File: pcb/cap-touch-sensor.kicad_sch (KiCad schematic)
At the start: 12 parts, among them U4 CAP1296-x-AIA

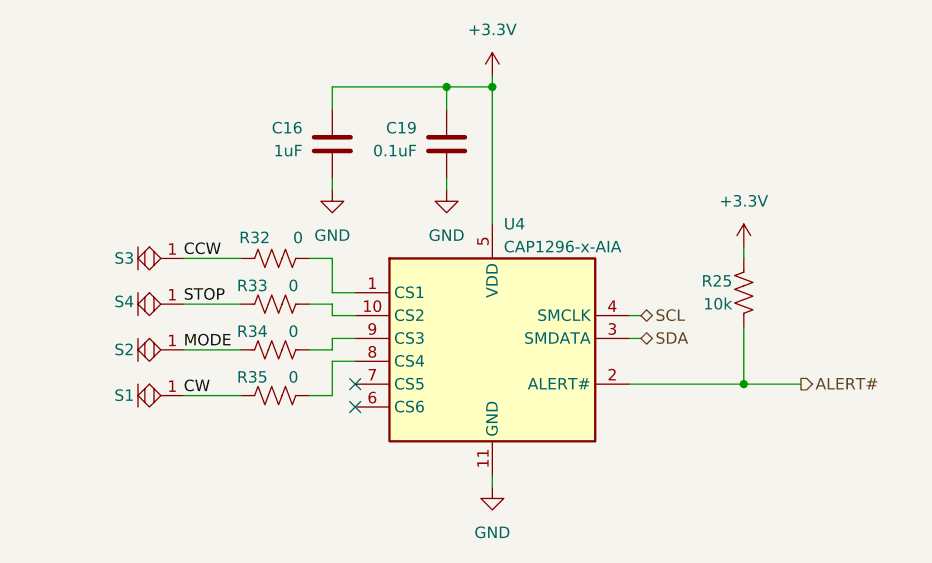
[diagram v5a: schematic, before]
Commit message: Some edits during PR review
- Silkscreen moved on board
- Get rid of value text in fab layer
- Invert TMC_EN name to indicate correct logic
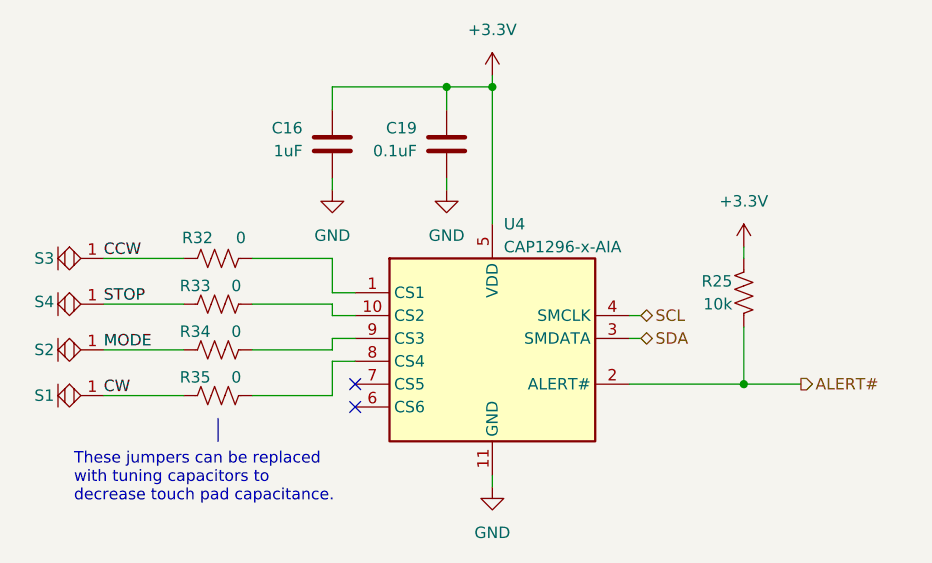
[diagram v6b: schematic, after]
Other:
- note added: "These jumpers can be replaced with tuning capacitors to decrease touch pad capacitance."
- moved on the sheet: R32, R33, R34, R35, S1, S2, S3, S4
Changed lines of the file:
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@@
 	(wire
 		(pts
-			(xy 67.31 74.93) (xy 73.66 74.93)
+			(xy 58.42 74.93) (xy 67.31 74.93)
 		)
 		(stroke
@@
 		)
 	)
+	(polyline
+		(pts
+			(xy 71.12 77.47) (xy 71.12 80.01)
+		)
+		(stroke
+			(width 0)
+			(type default)
+		)
+	)
 	(wire
 		(pts
@@
 	(wire
 		(pts
-			(xy 81.28 59.69) (xy 83.82 59.69)
+			(xy 74.93 59.69) (xy 83.82 59.69)
 		)
 		(stroke
@@
 	(wire
 		(pts
-			(xy 81.28 64.77) (xy 83.82 64.77)
+			(xy 74.93 64.77) (xy 83.82 64.77)
 		)
 		(stroke
@@
 	(wire
 		(pts
-			(xy 67.31 59.69) (xy 73.66 59.69)
+			(xy 58.42 59.69) (xy 67.31 59.69)
 		)
 		(stroke
@@
 	(wire
 		(pts
-			(xy 81.28 74.93) (xy 83.82 74.93)
-		)
-		(stroke
-			(width 0)
-			(type default)
-		)
-	)
-	(wire
-		(pts
-			(xy 67.31 64.77) (xy 73.66 64.77)
-		)
-		(stroke
-			(width 0)
-			(type default)
-		)
-	)
-	(wire
-		(pts
-			(xy 67.31 69.85) (xy 73.66 69.85)
+			(xy 74.93 74.93) (xy 83.82 74.93)
+		)
+		(stroke
+			(width 0)
+			(type default)
+		)
+	)
+	(wire
+		(pts
+			(xy 58.42 64.77) (xy 67.31 64.77)
+		)
+		(stroke
+			(width 0)
+			(type default)
+		)
+	)
+	(wire
+		(pts
+			(xy 58.42 69.85) (xy 67.31 69.85)
 		)
 		(stroke
@@
 	(wire
 		(pts
-			(xy 81.28 69.85) (xy 83.82 69.85)
+			(xy 74.93 69.85) (xy 83.82 69.85)
 		)
 		(stroke
@@
 		)
 	)
+	(text "These jumpers can be replaced\nwith tuning capacitors to \ndecrease touch pad capacitance."
+		(exclude_from_sim no)
+		(at 55.118 84.074 0)
+		(effects
+			(font
+				(size 1.27 1.27)
+			)
+			(justify left)
+		)
+	)
 	(label "MODE"
-		(at 67.31 69.85 0)
+		(at 58.42 69.85 0)
 		(fields_autoplaced yes)
 		(effects
@@
 	)
 	(label "CW"
-		(at 67.31 74.93 0)
+		(at 58.42 74.93 0)
 		(fields_autoplaced yes)
 		(effects
@@
 	)
 	(label "CCW"
-		(at 67.31 59.69 0)
+		(at 58.42 59.69 0)
 		(fields_autoplaced yes)
 		(effects
@@
 	)
 	(label "STOP"
-		(at 67.31 64.77 0)
+		(at 58.42 64.77 0)
 		(fields_autoplaced yes)
 		(effects
@@
 	(symbol
 		(lib_id "Device:R_US")
-		(at 77.47 59.69 90)
+		(at 71.12 59.69 90)
 		(unit 1)
 		(exclude_from_sim no)
@@
 		(dnp no)
 		(property "Reference" "R32"
-			(at 75.184 57.404 90)
+			(at 68.834 57.404 90)
 			(effects
 				(font
@@
 		)
 		(property "Value" "0"
-			(at 80.01 57.404 90)
+			(at 73.66 57.404 90)
 			(effects
 				(font
@@
 		)
 		(property "Footprint" "Resistor_SMD:R_0402_1005Metric"
-			(at 77.724 58.674 90)
+			(at 71.374 58.674 90)
 			(effects
 				(font
@@
 		)
 		(property "Datasheet" "~"
-			(at 77.47 59.69 0)
+			(at 71.12 59.69 0)
 			(effects
 				(font
@@
 		)
 		(property "Description" "Resistor, US symbol"
-			(at 77.47 59.69 0)
+			(at 71.12 59.69 0)
 			(effects
 				(font
@@
 	(symbol
 		(lib_id "open-ephys:TOUCH")
-		(at 64.77 64.77 90)
+		(at 55.88 64.77 90)
 		(mirror x)
 		(unit 1)
@@
 		(dnp no)
 		(property "Reference" "S4"
-			(at 60.706 64.516 90)
+			(at 51.816 64.516 90)
 			(effects
 				(font
@@
 		)
 		(property "Value" "~"
-			(at 63.5 62.23 90)
+			(at 54.61 62.23 90)
 			(effects
 				(font
@@
 		)
 		(property "Footprint" "open-ephys:Touch_Center_2mm"
-			(at 64.77 64.77 0)
+			(at 55.88 64.77 0)
 			(effects
 				(font
@@
 		)
 		(property "Datasheet" ""
-			(at 64.77 64.77 0)
+			(at 55.88 64.77 0)
 			(effects
 				(font
@@
 		)
 		(property "Description" "Printed capactitive touch sensor"
-			(at 64.77 64.77 0)
+			(at 55.88 64.77 0)
 			(effects
 				(font
@@
 	(symbol
 		(lib_id "open-ephys:TOUCH")
-		(at 64.77 69.85 90)
+		(at 55.88 69.85 90)
 		(mirror x)
 		(unit 1)
@@
 		(dnp no)
 		(property "Reference" "S2"
-			(at 60.706 69.85 90)
+			(at 51.816 69.85 90)
 			(effects
 				(font
@@
 		)
 		(property "Value" "~"
-			(at 63.5 67.31 90)
+			(at 54.61 67.31 90)
 			(effects
 				(font
@@
 		)
 		(property "Footprint" "open-ephys:Touch_Center_2mm"
-			(at 64.77 69.85 0)
+			(at 55.88 69.85 0)
 			(effects
 				(font
@@
 		)
 		(property "Datasheet" ""
-			(at 64.77 69.85 0)
+			(at 55.88 69.85 0)
 			(effects
 				(font
@@
 		)
 		(property "Description" "Printed capactitive touch sensor"
-			(at 64.77 69.85 0)
+			(at 55.88 69.85 0)
 			(effects
 				(font
@@
 	(symbol
 		(lib_id "open-ephys:TOUCH")
-		(at 64.77 59.69 90)
+		(at 55.88 59.69 90)
 		(mirror x)
 		(unit 1)
@@
 		(dnp no)
 		(property "Reference" "S3"
-			(at 60.706 59.69 90)
+			(at 51.816 59.69 90)
 			(effects
 				(font
@@
 		)
 		(property "Value" "~"
-			(at 63.5 57.15 90)
+			(at 54.61 57.15 90)
 			(effects
 				(font
@@
 		)
 		(property "Footprint" "open-ephys:Touch_Center_2mm"
-			(at 64.77 59.69 0)
+			(at 55.88 59.69 0)
 			(effects
 				(font
@@
 		)
 		(property "Datasheet" ""
-			(at 64.77 59.69 0)
+			(at 55.88 59.69 0)
 			(effects
 				(font
@@
 		)
 		(property "Description" "Printed capactitive touch sensor"
-			(at 64.77 59.69 0)
+			(at 55.88 59.69 0)
 			(effects
 				(font
@@
 	(symbol
 		(lib_id "Device:R_US")
-		(at 77.47 74.93 90)
+		(at 71.12 74.93 90)
 		(unit 1)
 		(exclude_from_sim no)
@@
 		(dnp no)
 		(property "Reference" "R35"
-			(at 74.93 72.898 90)
+			(at 68.58 72.898 90)
 			(effects
 				(font
@@
 		)
 		(property "Value" "0"
-			(at 79.502 72.898 90)
+			(at 73.152 72.898 90)
 			(effects
 				(font
@@
 		)
 		(property "Footprint" "Resistor_SMD:R_0402_1005Metric"
-			(at 77.724 73.914 90)
+			(at 71.374 73.914 90)
 			(effects
 				(font
@@
 		)
 		(property "Datasheet" "~"
-			(at 77.47 74.93 0)
+			(at 71.12 74.93 0)
 			(effects
 				(font
@@
 		)
 		(property "Description" "Resistor, US symbol"
-			(at 77.47 74.93 0)
+			(at 71.12 74.93 0)
 			(effects
 				(font
@@
 	(symbol
 		(lib_id "Device:R_US")
-		(at 77.47 69.85 90)
+		(at 71.12 69.85 90)
 		(unit 1)
 		(exclude_from_sim no)
@@
 		(dnp no)
 		(property "Reference" "R34"
-			(at 74.93 67.818 90)
+			(at 68.58 67.818 90)
 			(effects
 				(font
@@
 		)
 		(property "Value" "0"
-			(at 79.502 67.818 90)
+			(at 73.152 67.818 90)
 			(effects
 				(font
@@
 		)
 		(property "Footprint" "Resistor_SMD:R_0402_1005Metric"
-			(at 77.724 68.834 90)
+			(at 71.374 68.834 90)
 			(effects
 				(font
@@
 		)
 		(property "Datasheet" "~"
-			(at 77.47 69.85 0)
+			(at 71.12 69.85 0)
 			(effects
 				(font
@@
 		)
 		(property "Description" "Resistor, US symbol"
-			(at 77.47 69.85 0)
+			(at 71.12 69.85 0)
 			(effects
 				(font
@@
 	(symbol
 		(lib_id "Device:R_US")
-		(at 77.47 64.77 90)
+		(at 71.12 64.77 90)
 		(unit 1)
 		(exclude_from_sim no)
@@
 		(dnp no)
 		(property "Reference" "R33"
-			(at 74.93 62.738 90)
+			(at 68.58 62.738 90)
 			(effects
 				(font
@@
 		)
 		(property "Value" "0"
-			(at 79.502 62.738 90)
+			(at 73.152 62.738 90)
 			(effects
 				(font
@@
 		)
 		(property "Footprint" "Resistor_SMD:R_0402_1005Metric"
-			(at 77.724 63.754 90)
+			(at 71.374 63.754 90)
 			(effects
 				(font
@@
 		)
 		(property "Datasheet" "~"
-			(at 77.47 64.77 0)
+			(at 71.12 64.77 0)
 			(effects
 				(font
@@
 		)
 		(property "Description" "Resistor, US symbol"
-			(at 77.47 64.77 0)
+			(at 71.12 64.77 0)
 			(effects
 				(font
@@
 	(symbol
 		(lib_id "open-ephys:TOUCH")
-		(at 64.77 74.93 90)
+		(at 55.88 74.93 90)
 		(mirror x)
 		(unit 1)
@@
 		(dnp no)
 		(property "Reference" "S1"
-			(at 60.706 74.93 90)
+			(at 51.816 74.93 90)
 			(effects
 				(font
@@
 		)
 		(property "Value" "~"
-			(at 63.5 72.39 90)
+			(at 54.61 72.39 90)
 			(effects
 				(font
@@
 		)
 		(property "Footprint" "open-ephys:Touch_Center_2mm"
-			(at 64.77 74.93 0)
+			(at 55.88 74.93 0)
 			(effects
 				(font
@@
 		)
 		(property "Datasheet" ""
-			(at 64.77 74.93 0)
+			(at 55.88 74.93 0)
 			(effects
 				(font
@@
 		)
 		(property "Description" "Printed capactitive touch sensor"
-			(at 64.77 74.93 0)
-			(effects
-				(font
+			(at 55.88 74.93 0)
+			(effects
+				(font

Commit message: Change touch sensor series caps 0402 ->0805
- Also, move uart traces to prevent xtal and button to
  couple capacitatively
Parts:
- R32, R33, R34, R35: footprint Resistor_SMD:R_0402_1005Metric -> Resistor_SMD:R_0805_2012Metric
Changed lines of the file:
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@@
 			)
 		)
-		(property "Footprint" "Resistor_SMD:R_0402_1005Metric"
+		(property "Footprint" "Resistor_SMD:R_0805_2012Metric"
 			(at 71.374 58.674 90)
 			(effects
@@
 			)
 		)
-		(property "Footprint" "Resistor_SMD:R_0402_1005Metric"
+		(property "Footprint" "Resistor_SMD:R_0805_2012Metric"
 			(at 71.374 73.914 90)
 			(effects
@@
 			)
 		)
-		(property "Footprint" "Resistor_SMD:R_0402_1005Metric"
+		(property "Footprint" "Resistor_SMD:R_0805_2012Metric"
 			(at 71.374 68.834 90)
 			(effects
@@
 			)
 		)
-		(property "Footprint" "Resistor_SMD:R_0402_1005Metric"
+		(property "Footprint" "Resistor_SMD:R_0805_2012Metric"
 			(at 71.374 63.754 90)
 			(effects
